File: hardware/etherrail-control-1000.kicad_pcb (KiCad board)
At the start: 2 copper layers, 15.9 x 27.9 mm, 33 parts, among them J1 Conn_02x04_Odd_Even, J2 Conn_01x04, U1 AMS1117-3.3, U2 ESP32-C3, Y2 Crystal_GND24

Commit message: WIP: Add revised hardware
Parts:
- removed D5: D, Diode_SMD:D_SOD-323
- removed D8: Yellow, LED_SMD:LED_0603_1608Metric
- removed U1: AMS1117-3.3, Package_TO_SOT_SMD:SOT-89-3
- added 3VR1: ME6118, Package_TO_SOT_SMD:SOT-89-3, B.Cu at (35.6, 40.1)
- added 6VR1: 78N06G, Package_TO_SOT_SMD:SOT-89-3, B.Cu at (30.5, 40.1)
- added ?: Yellow, LED_SMD:LED_0603_1608Metric, F.Cu at (38.9, 37.6)
- added C14: 1mF 6.3V, Capacitor_Tantalum_SMD:CP_EIA-7343-43_Kemet-X, F.Cu at (30.5, 36.1)
- added JP1: Jumper_2_Open, Jumper:SolderJumper-2_P1.3mm_Open_Pad1.0x1.5mm, F.Cu at (39.6, 43.4)
- added JP2: Jumper_2_Open, Jumper:SolderJumper-2_P1.3mm_Open_Pad1.0x1.5mm, F.Cu at (39.6, 47.0)
- added Q1: AO3400A, Package_TO_SOT_SMD:SOT-23, B.Cu at (38.1, 33.5)
- added Q2: AO3400A, Package_TO_SOT_SMD:SOT-23, B.Cu at (27.9, 33.5)
- added R5: 100k, Resistor_SMD:R_0402_1005Metric, B.Cu at (33.0, 36.3)
- added R6: 10k, Resistor_SMD:R_0201_0603Metric, F.Cu at (36.6, 45.8)
- added R7: 22, Resistor_SMD:R_0201_0603Metric, F.Cu at (29.2, 46.8)
- added R8: 5.1k, Resistor_SMD:R_0201_0603Metric, F.Cu at (36.6, 44.0)
- C1: value 100uF -> 1mF 6.3V; footprint Capacitor_Tantalum_SMD:CP_EIA-7343-30_AVX-N -> Capacitor_Tantalum_SMD:CP_EIA-7343-43_Kemet-X
- J2: footprint Connector_PinHeader_1.00mm:PinHeader_1x04_P1.00mm_Vertical -> Connector_PinHeader_1.27mm:PinHeader_1x04_P1.27mm_Vertical
- U3: moved to B.Cu
- Y2: value Crystal_GND24 -> 40.000MHz 15pF
- moved D3 90.7 mm to (26.2, 27.2), turned to 90 degrees
- moved D4 89.9 mm to (26.2, 30.5), turned to 90 degrees
- moved J1 84.1 mm to (29.2, 29.7), turned to 90 degrees
- moved R4 78.3 mm to (38.9, 39.6), turned to 0 degrees
- moved C5 77.5 mm to (36.6, 47.3), turned to -90 degrees
- moved D6 77.5 mm to (26.2, 33.8), turned to 90 degrees
- moved C7 77.3 mm to (28.5, 49.5), turned to 180 degrees
- moved R1 77.2 mm to (39.1, 33.0)
- moved U2 77.1 mm to (33.0, 46.0)
- moved C6 76.8 mm to (37.3, 44.0), turned to -90 degrees
- moved J2 76.7 mm to (26.4, 39.4), turned to 0 degrees
- moved AE1 76.6 mm to (33.0, 52.3)
- moved Y2 76.4 mm to (27.0, 46.9)
- moved C8 75.8 mm to (30.0, 49.5)
- moved C13 75.7 mm to (28.5, 50.5), turned to 180 degrees
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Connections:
- C1 pad 1: Net-(D5-K) -> Net-(3VR1-VI)
- C9 pad 1: Net-(U2-XTAL_P) -> Net-(C9-Pad1)
- D1 pad 1: /Unfiltered Power In -> /Light Common (+)
- D4 pad 1: /Unfiltered Power In -> /Light Common (+)
- D6 pad 1: Net-(D5-K) -> Net-(6VR1-VI)
- D6 pad 2: /Unfiltered Power In -> /Light Common (+)
- J2 pad 1: /USB Power In -> /Light Common (+)
- J2 pad 2: /USB Data Positive -> /USB Data Negative
- J2 pad 3: /USB Data Negative -> /USB Data Positive
- R1 pad 1: /Unfiltered Power In -> /Light Common (+)
- R4 pad 1: Net-(U2-GPIO8) -> Net-(U2-GPIO10)
- U2 pad 14: Net-(U2-GPIO8) -> /Download Enable
- U2 pad 15: unconnected-(U2-GPIO9/BOOT-Pad15) -> /Bootmode
- U2 pad 16: unconnected-(U2-GPIO10-Pad16) -> Net-(U2-GPIO10)
- U2 pad 21: unconnected-(U2-SPICS0/GPIO14-Pad21) -> /Logic Level Light Front
- U2 pad 22: unconnected-(U2-SPICLK/GPIO15-Pad22) -> /Logic Level Light Rear
- U2 pad 23: /Motor Controlling Direction -> /Motor Controlling PWM
- U2 pad 24: /Motor Controlling PWM -> /Motor Controlling Direction
- U3 pad 4: /Unfiltered Power In -> /Light Common (+)
- Y2 pad 3: Net-(U2-XTAL_P) -> Net-(C9-Pad1)
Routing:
- net /Unfiltered Power In: track 26.7 -> 0.00 mm
- net /Light Common (+): track 0.00 -> 22.8 mm, vias 0 -> 1
- net Net-(3VR1-VI): track 0.00 -> 17.0 mm, vias 0 -> 1
- net /Motor Positive: track 21.0 -> 4.83 mm, vias 2 -> 0
- net Net-(D5-K): track 15.7 -> 0.00 mm, vias 2 -> 0
- net /Controller Power: track 51.8 -> 36.3 mm
- net /Logic Level Light Front: track 0.00 -> 13.4 mm, vias 0 -> 1
- net /Logic Level Light Rear: track 0.00 -> 12.4 mm, vias 0 -> 1
- net /Motor Controlling PWM: track 3.74 -> 14.2 mm, vias 0 -> 1
- net /Motor Controlling Direction: track 4.94 -> 14.6 mm, vias 0 -> 1
- net /Light Front (-): track 0.00 -> 7.96 mm, vias 0 -> 1
- net Net-(6VR1-VI): track 0.00 -> 7.78 mm, vias 0 -> 1
- net Net-(U2-GPIO8): track 7.20 -> 0.00 mm
- net /Light Rear (-): track 0.00 -> 6.66 mm, vias 0 -> 1
- net Net-(U2-GPIO10): track 0.00 -> 6.62 mm, vias 0 -> 2
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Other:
- board size 15.9 x 27.9 mm -> 16 x 27.9 mm
- board text added: "EtherRail"
- board text added: "TC800N652+D+CA+M2"
- board text added: "v0.2.0"
- board text removed: "Control 1000 v0.1.0 D8SP"

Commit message: Fix rename product
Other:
- board text added: "TC800N652+D+CA+2B"
- board text removed: "TC800N652+D+CA+M2"

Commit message: Add EN jumper
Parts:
- added C15: 100n, Capacitor_SMD:C_0201_0603Metric, F.Cu at (37.9, 50.2)
- added JP3: Jumper_2_Open, Jumper:SolderJumper-2_P1.3mm_Open_Pad1.0x1.5mm, F.Cu at (39.6, 49.9)
- added R9: 5.1k, Resistor_SMD:R_0201_0603Metric, F.Cu at (37.9, 48.5)
- moved JP2 0.62 mm to (39.6, 46.4)
- moved JP1 0.62 mm to (39.6, 42.8)
- moved C4 0.25 mm to (35.1, 50.3)
- gave numbers to parts that had none: 1
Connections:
- U2 pad 7: /Controller Power -> /Enable
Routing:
- net /Enable: track 0.00 -> 8.76 mm
- net GND: track 34.0 -> 32.0 mm, vias 12 -> 14
- net /Controller Power: track 36.3 -> 35.4 mm

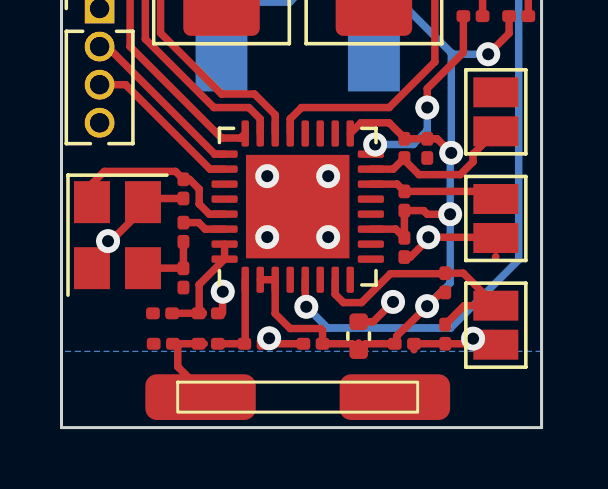
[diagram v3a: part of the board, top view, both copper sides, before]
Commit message: Add GPIO2 rotue
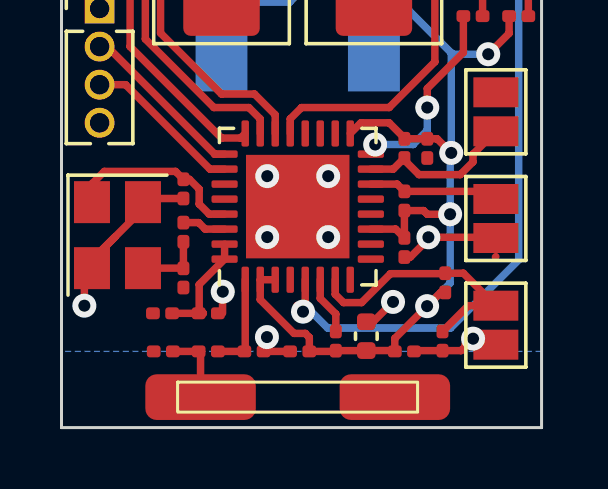
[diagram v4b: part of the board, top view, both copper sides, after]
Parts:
- added R10: 5.1k, Resistor_SMD:R_0201_0603Metric, F.Cu at (34.3, 50.5)
- R6: value 10k -> 5.1k
- moved C2 0.51 mm to (33.1, 50.8)
- moved C12 0.25 mm to (31.6, 50.8)
- moved C13 0.25 mm to (28.5, 50.8)
- moved C3 0.25 mm to (36.6, 50.8)
- moved C4 0.25 mm to (35.3, 50.3)
- moved L1 0.25 mm to (30.0, 50.8)
- moved C15 0.25 mm to (37.8, 50.5)
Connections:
- U2 pad 6: unconnected-(U2-GPIO2/ADC1_CH2-Pad6) -> Net-(U2-GPIO2/ADC1_CH2)
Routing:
- net GND: track 32.0 -> 34.1 mm
- net Net-(U2-GPIO2/ADC1_CH2): track 0.00 -> 1.94 mm
- net /Power Sensing Input: track 25.3 -> 25.8 mm

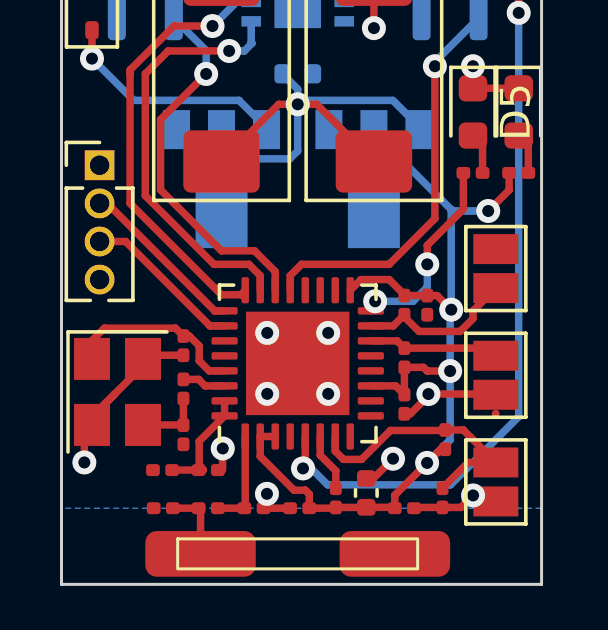
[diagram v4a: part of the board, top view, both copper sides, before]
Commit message: Fix use ESP32-C3 with flash (C3-FH4)
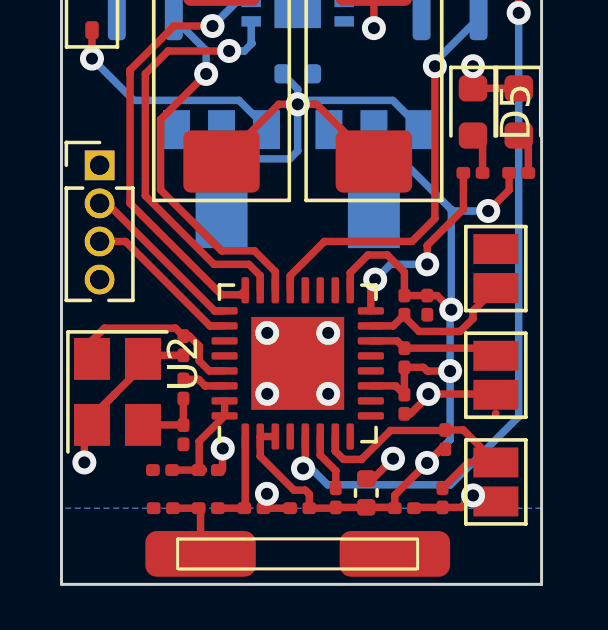
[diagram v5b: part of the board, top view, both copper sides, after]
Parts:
- U2: value ESP32-C3 -> ESP32-C3FH4; footprint Package_DFN_QFN:QFN-32-1EP_5x5mm_P0.5mm_EP3.45x3.45mm -> Package_DFN_QFN:QFN-32-1EP_5x5mm_P0.5mm_EP3.1x3.1mm
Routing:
- net /Controller Power: track 35.8 -> 37.3 mm
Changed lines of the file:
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@@
     )
   )
-  (footprint "Package_DFN_QFN:QFN-32-1EP_5x5mm_P0.5mm_EP3.45x3.45mm" (layer "F.Cu")
+  (footprint "Package_DFN_QFN:QFN-32-1EP_5x5mm_P0.5mm_EP3.1x3.1mm" (layer "F.Cu")
     (at 33.02 45.974 90)
-    (descr "QFN, 32 Pin (http://www.analog.com/media/en/package-pcb-resources/package/pkg_pdf/ltc-legacy-qfn/QFN_32_05-08-1693.pdf), generated with kicad-footprint-generator ipc_noLead_generator.py")
+    (descr "QFN, 32 Pin (http://ww1.microchip.com/downloads/en/DeviceDoc/8008S.pdf#page=20), generated with kicad-footprint-generator ipc_noLead_generator.py")
     (tags "QFN NoLead")
-    (property "LCSC" "C2838500")
+    (property "LCSC" "C2858491")
     (property "Sheetfile" "etherrail-control-1000.kicad_sch")
     (property "Sheetname" "")
     (property "ki_description" "ESP32-C3 family is an ultra-low-power MCU-based SoC solution that supports 2.4 GHz Wi-Fi and Bluetooth®Low Energy (Bluetooth LE).")
     (attr smd)
-    (fp_text reference "U2" (at 0 -3.82 90) (layer "F.SilkS") hide
+    (fp_text reference "U2" (at 0 -3.82 90) (layer "F.SilkS")
         (effects (font (size 1 1) (thickness 0.15)))
     )
-    (fp_text value "ESP32-C3" (at 0 3.82 90) (layer "F.Fab")
+    (fp_text value "ESP32-C3FH4" (at 0 3.82 90) (layer "F.Fab")
         (effects (font (size 1 1) (thickness 0.15)))
     )
@@
     (fp_line (start 2.5 2.5) (end -2.5 2.5)
       (stroke (width 0.1) (type solid)) (layer "F.Fab"))
-    (pad "" smd roundrect (at -1.15 -1.15 90) (size 0.93 0.93) (layers "F.Paste") (roundrect_rratio 0.25))
-    (pad "" smd roundrect (at -1.15 0 90) (size 0.93 0.93) (layers "F.Paste") (roundrect_rratio 0.25))
-    (pad "" smd roundrect (at -1.15 1.15 90) (size 0.93 0.93) (layers "F.Paste") (roundrect_rratio 0.25))
-    (pad "" smd roundrect (at 0 -1.15 90) (size 0.93 0.93) (layers "F.Paste") (roundrect_rratio 0.25))
-    (pad "" smd roundrect (at 0 0 90) (size 0.93 0.93) (layers "F.Paste") (roundrect_rratio 0.25))
-    (pad "" smd roundrect (at 0 1.15 90) (size 0.93 0.93) (layers "F.Paste") (roundrect_rratio 0.25))
-    (pad "" smd roundrect (at 1.15 -1.15 90) (size 0.93 0.93) (layers "F.Paste") (roundrect_rratio 0.25))
-    (pad "" smd roundrect (at 1.15 0 90) (size 0.93 0.93) (layers "F.Paste") (roundrect_rratio 0.25))
-    (pad "" smd roundrect (at 1.15 1.15 90) (size 0.93 0.93) (layers "F.Paste") (roundrect_rratio 0.25))
+    (pad "" smd roundrect (at -1.03 -1.03 90) (size 0.83 0.83) (layers "F.Paste") (roundrect_rratio 0.25))
+    (pad "" smd roundrect (at -1.03 0 90) (size 0.83 0.83) (layers "F.Paste") (roundrect_rratio 0.25))
+    (pad "" smd roundrect (at -1.03 1.03 90) (size 0.83 0.83) (layers "F.Paste") (roundrect_rratio 0.25))
+    (pad "" smd roundrect (at 0 -1.03 90) (size 0.83 0.83) (layers "F.Paste") (roundrect_rratio 0.25))
+    (pad "" smd roundrect (at 0 0 90) (size 0.83 0.83) (layers "F.Paste") (roundrect_rratio 0.25))
+    (pad "" smd roundrect (at 0 1.03 90) (size 0.83 0.83) (layers "F.Paste") (roundrect_rratio 0.25))
+    (pad "" smd roundrect (at 1.03 -1.03 90) (size 0.83 0.83) (layers "F.Paste") (roundrect_rratio 0.25))
+    (pad "" smd roundrect (at 1.03 0 90) (size 0.83 0.83) (layers "F.Paste") (roundrect_rratio 0.25))
+    (pad "" smd roundrect (at 1.03 1.03 90) (size 0.83 0.83) (layers "F.Paste") (roundrect_rratio 0.25))
     (pad "1" smd roundrect (at -2.4375 -1.75 90) (size 0.875 0.25) (layers "F.Cu" "F.Paste" "F.Mask") (roundrect_rratio 0.25)
       (net 8 "/Antenna") (pinfunction "LNA_IN") (pintype "bidirectional"))
@@
     (pad "32" smd roundrect (at -1.75 -2.4375 90) (size 0.25 0.875) (layers "F.Cu" "F.Paste" "F.Mask") (roundrect_rratio 0.25)
       (net 4 "/Controller Power") (pinfunction "VDDA") (pintype "passive"))
-    (pad "33" smd rect (at 0 0 90) (size 3.45 3.45) (layers "F.Cu" "F.Mask")
+    (pad "33" smd rect (at 0 0 90) (size 3.1 3.1) (layers "F.Cu" "F.Mask")
       (net 3 "GND") (pinfunction "GND") (pintype "power_in"))
-    (model "${KICAD6_3DMODEL_DIR}/Package_DFN_QFN.3dshapes/QFN-32-1EP_5x5mm_P0.5mm_EP3.45x3.45mm.wrl"
+    (model "${KICAD6_3DMODEL_DIR}/Package_DFN_QFN.3dshapes/QFN-32-1EP_5x5mm_P0.5mm_EP3.1x3.1mm.wrl"
       (offset (xyz 0 0 0))
       (scale (xyz 1 1 1))
@@
   (via (at 25.908 49.276) (size 0.8) (drill 0.4) (layers "F.Cu" "B.Cu") (net 3))
   (via (at 34.036 44.958) (size 0.8) (drill 0.4) (layers "F.Cu" "B.Cu") (net 3))
-  (segment (start 36.068 43.18) (end 36.576 43.688) (width 0.25) (layer "F.Cu") (net 4))
   (segment (start 33.406 50.332112) (end 33.406 50.8) (width 0.25) (layer "F.Cu") (net 4))
   (segment (start 37.789985 48.834) (end 37.937 48.834) (width 0.25) (layer "F.Cu") (net 4))
+  (segment (start 34.77 42.954) (end 35.364 42.36) (width 0.25) (layer "F.Cu") (net 4))
   (segment (start 33.406 50.8) (end 34.265 50.8) (width 0.25) (layer "F.Cu") (net 4))
   (segment (start 35.4575 46.724) (end 36.285 46.724) (width 0.25) (layer "F.Cu") (net 4))
-  (segment (start 35.1265 43.18) (end 36.068 43.18) (width 0.25) (layer "F.Cu") (net 4))
   (segment (start 34.29 50.775) (end 35.303 50.775) (width 0.25) (layer "F.Cu") (net 4))
   (segment (start 37.338 46.228) (end 37.216 46.106) (width 0.25) (layer "F.Cu") (net 4))
@@
   (segment (start 36.228 50.772) (end 36.256 50.8) (width 0.25) (layer "F.Cu") (net 4))
   (segment (start 37.216 46.106) (end 36.576 46.106) (width 0.25) (layer "F.Cu") (net 4))
+  (segment (start 35.364 42.36) (end 36.01 42.36) (width 0.25) (layer "F.Cu") (net 4))
   (segment (start 29.875 49.53) (end 29.735 49.39) (width 0.25) (layer "F.Cu") (net 4))
   (segment (start 33.274 50.200112) (end 33.406 50.332112) (width 0.25) (layer "F.Cu") (net 4))
@@
   (segment (start 36.285 46.724) (end 36.576 47.015) (width 0.25) (layer "F.Cu") (net 4))
   (segment (start 31.77 48.4115) (end 31.77 49.074129) (width 0.25) (layer "F.Cu") (net 4))
-  (segment (start 36.576 43.688) (end 36.576 43.713) (width 0.25) (layer "F.Cu") (net 4))
+  (segment (start 34.77 43.5365) (end 34.77 42.954) (width 0.25) (layer "F.Cu") (net 4))
+  (segment (start 36.01 42.36) (end 36.576 42.926) (width 0.25) (layer "F.Cu") (net 4))
+  (segment (start 36.576 42.926) (end 36.576 43.713) (width 0.25) (layer "F.Cu") (net 4))
   (segment (start 32.895983 50.200112) (end 33.274 50.200112) (width 0.25) (layer "F.Cu") (net 4))
   (segment (start 35.303 50.775) (end 35.306 50.772) (width 0.25) (layer "F.Cu") (net 4))
@@
   (segment (start 36.256 50.367985) (end 37.33262 49.291365) (width 0.25) (layer "F.Cu") (net 4))
   (segment (start 31.77 49.074129) (end 32.895983 50.200112) (width 0.25) (layer "F.Cu") (net 4))
-  (segment (start 34.77 43.5365) (end 35.1265 43.18) (width 0.25) (layer "F.Cu") (net 4))
   (segment (start 37.33262 49.291365) (end 37.789985 48.834) (width 0.25) (layer "F.Cu") (net 4))
   (segment (start 35.306 50.772) (end 36.228 50.772) (width 0.25) (layer "F.Cu") (net 4))
@@
   (segment (start 36.576 44.422042) (end 37.062458 44.9085) (width 0.25) (layer "F.Cu") (net 20))
   (segment (start 38.862281 44.225719) (end 39.624 43.464) (width 0.25) (layer "F.Cu") (net 20))
-  (segment (start 32.77 43.04926) (end 33.14726 42.672) (width 0.25) (layer "F.Cu") (net 26))
-  (segment (start 32.77 43.5365) (end 32.77 43.04926) (width 0.25) (layer "F.Cu") (net 26))
-  (segment (start 33.14726 42.672) (end 36.068 42.672) (width 0.25) (layer "F.Cu") (net 26))
-  (segment (start 36.068 42.672) (end 37.592 41.148) (width 0.25) (layer "F.Cu") (net 26))
+  (segment (start 33.90926 41.91) (end 36.83 41.91) (width 0.25) (layer "F.Cu") (net 26))
   (segment (start 37.592 41.148) (end 37.592 36.068) (width 0.25) (layer "F.Cu") (net 26))
+  (segment (start 32.77 43.5365) (end 32.77 43.04926) (width 0.25) (layer "F.Cu") (net 26))
+  (segment (start 36.83 41.91) (end 37.592 41.148) (width 0.25) (layer "F.Cu") (net 26))
+  (segment (start 32.77 43.04926) (end 33.90926 41.91) (width 0.25) (layer "F.Cu") (net 26))
   (via (at 37.592 36.068) (size 0.8) (drill 0.4) (layers "F.Cu" "B.Cu") (net 26))
   (segment (start 37.592 35.9235) (end 39.05 34.4655) (width 0.25) (layer "B.Cu") (net 26))
@@
   (segment (start 39.182 39.624) (end 39.182 38.6995) (width 0.25) (layer "F.Cu") (net 41))
   (segment (start 39.182 38.6995) (end 38.862 38.3795) (width 0.25) (layer "F.Cu") (net 41))
-  (segment (start 35.4575 44.224) (end 35.4575 44.048549) (width 0.25) (layer "F.Cu") (net 42))
   (segment (start 37.338 42.038396) (end 38.542 40.834396) (width 0.25) (layer "F.Cu") (net 42))
-  (segment (start 35.4575 44.048549) (end 35.601549 43.9045) (width 0.25) (layer "F.Cu") (net 42))
+  (segment (start 35.601549 43.18) (end 35.4575 43.324049) (width 0.25) (layer "F.Cu") (net 42))
   (segment (start 37.338 42.672) (end 37.338 42.038396) (width 0.25) (layer "F.Cu") (net 42))
+  (segment (start 35.4575 43.324049) (end 35.4575 44.224) (width 0.25) (layer "F.Cu") (net 42))
   (segment (start 38.542 40.834396) (end 38.542 39.624) (width 0.25) (layer "F.Cu") (net 42))
-  (via (at 35.601549 43.9045) (size 0.8) (drill 0.4) (layers "F.Cu" "B.Cu") (net 42))
+  (via (at 35.601549 43.18) (size 0.8) (drill 0.4) (layers "F.Cu" "B.Cu") (net 42))
   (via (at 37.338 42.672) (size 0.8) (drill 0.4) (layers "F.Cu" "B.Cu") (net 42))
-  (segment (start 35.601549 43.9045) (end 36.8675 43.9045) (width 0.25) (layer "B.Cu") (net 42))
-  (segment (start 37.338 43.434) (end 37.338 42.672) (width 0.25) (layer "B.Cu") (net 42))
-  (segment (start 36.8675 43.9045) (end 37.338 43.434) (width 0.25) (layer "B.Cu") (net 42))
+  (segment (start 35.601549 43.18) (end 36.109549 42.672) (width 0.25) (layer "B.Cu") (net 42))
+  (segment (start 36.109549 42.672) (end 37.338 42.672) (width 0.25) (layer "B.Cu") (net 42))
   (segment (start 38.705 49.276) (end 39.624 49.276) (width 0.25) (layer "F.Cu") (net 43))
   (segment (start 37.937 48.194) (end 38.542 48.194) (width 0.25) (layer "F.Cu") (net 43))

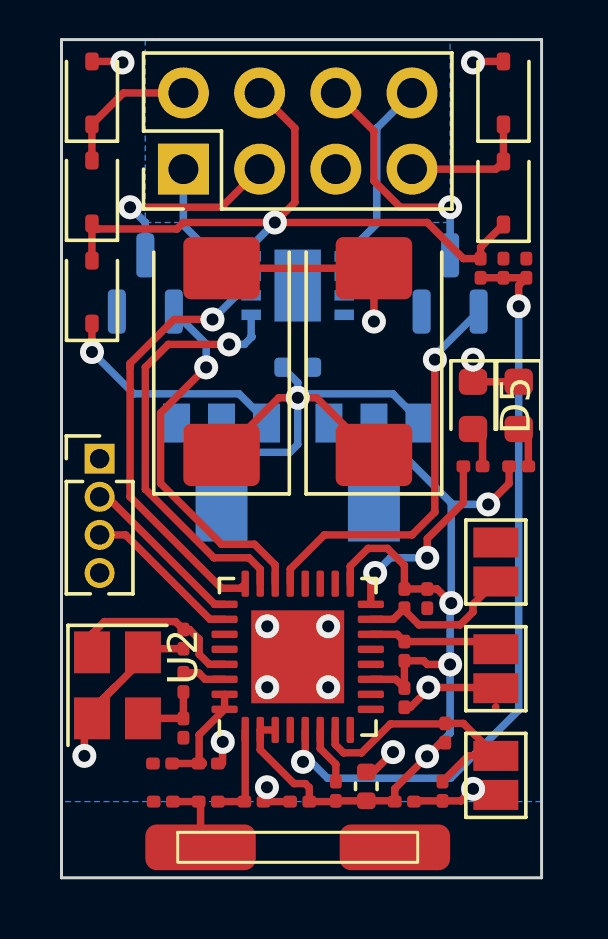
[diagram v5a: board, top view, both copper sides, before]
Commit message: Fix connected paths
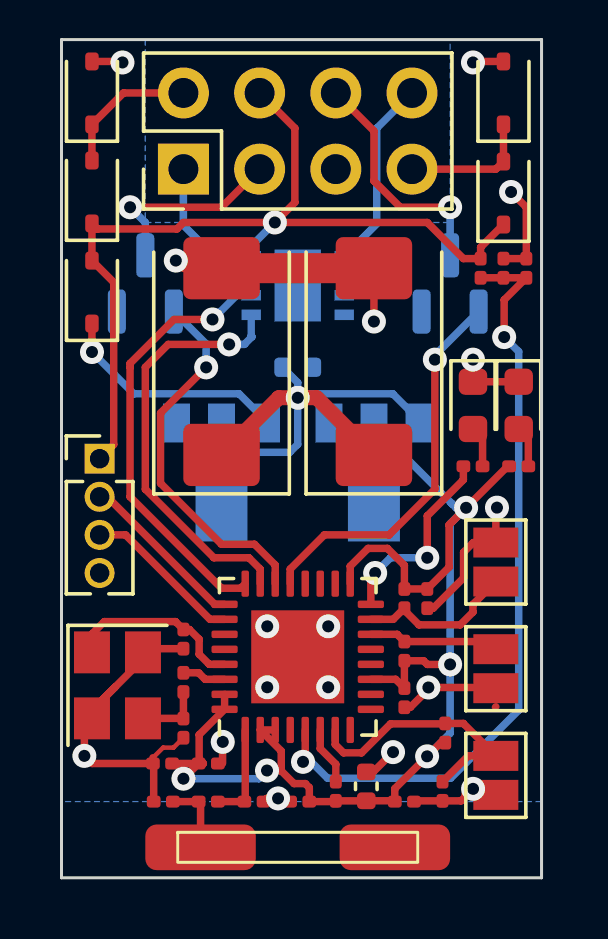
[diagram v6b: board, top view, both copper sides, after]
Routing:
- net GND: track 34.1 -> 49.0 mm, vias 14 -> 17
- net /Light Common (+): track 22.8 -> 29.9 mm
- net /Controller Power: track 37.3 -> 43.5 mm, vias 4 -> 5
